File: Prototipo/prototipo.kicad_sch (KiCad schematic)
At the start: 13 parts, among them J1 Conn_01x02_Socket, J4 Conn_01x12_Pin

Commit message: cambio el zener y subo la listita de compras
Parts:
- J1: footprint TerminalBlock:TerminalBlock_MaiXu_MX126-5.0-02P_1x02_P5.00mm -> Huellas:TerminalBlock_bornier-2_P5.08mm
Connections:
- net GND is gone; now on net 0: A1.7 (GND), J4.1 (Pin_1), J4.12 (Pin_12)
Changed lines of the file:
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@@
+	(wire
+		(pts
+			(xy 147.32 175.26) (xy 146.05 175.26)
+		)
+		(stroke
+			(width 0)
+			(type default)
+		)
+	)
 	(wire
 		(pts
@@
 	(wire
 		(pts
-			(xy 146.05 175.26) (xy 148.59 175.26)
-		)
-		(stroke
-			(width 0)
-			(type default)
-		)
-	)
-	(wire
-		(pts
 			(xy 242.57 60.96) (xy 247.65 60.96)
 		)
@@
 		(pts
 			(xy 87.63 60.96) (xy 163.83 60.96)
+		)
+		(stroke
+			(width 0)
+			(type default)
+		)
+	)
+	(wire
+		(pts
+			(xy 147.32 180.34) (xy 147.32 175.26)
 		)
 		(stroke
@@
 				(path "/c9225433-a7fd-41e8-8162-e91e829dcb79"
 					(reference "#GND017")
-					(unit 1)
-				)
-			)
-		)
-	)
-	(symbol
-		(lib_id "power:GND")
-		(at 148.59 175.26 0)
-		(unit 1)
-		(exclude_from_sim no)
-		(in_bom yes)
-		(on_board yes)
-		(dnp no)
-		(fields_autoplaced yes)
-		(property "Reference" "#PWR01"
-			(at 148.59 181.61 0)
-			(effects
-				(font
-					(size 1.27 1.27)
-				)
-				(hide yes)
-			)
-		)
-		(property "Value" "GND"
-			(at 148.59 180.34 0)
-			(effects
-				(font
-					(size 1.27 1.27)
-				)
-			)
-		)
-		(property "Footprint" ""
-			(at 148.59 175.26 0)
-			(effects
-				(font
-					(size 1.27 1.27)
-				)
-				(hide yes)
-			)
-		)
-		(property "Datasheet" ""
-			(at 148.59 175.26 0)
-			(effects
-				(font
-					(size 1.27 1.27)
-				)
-				(hide yes)
-			)
-		)
-		(property "Description" "Power symbol creates a global label with name \"GND\" , ground"
-			(at 148.59 175.26 0)
-			(effects
-				(font
-					(size 1.27 1.27)
-				)
-				(hide yes)
-			)
-		)
-		(pin "1"
-		)
-		(instances
-			(project ""
-				(path "/c9225433-a7fd-41e8-8162-e91e829dcb79"
-					(reference "#PWR01")
 					(unit 1)
 				)
@@
 	)
 	(symbol
-		(lib_id "power:GND")
-		(at 88.9 182.88 0)
-		(unit 1)
-		(exclude_from_sim no)
-		(in_bom yes)
-		(on_board yes)
-		(dnp no)
-		(fields_autoplaced yes)
-		(property "Reference" "#PWR02"
-			(at 88.9 189.23 0)
-			(effects
-				(font
-					(size 1.27 1.27)
-				)
-				(hide yes)
-			)
-		)
-		(property "Value" "GND"
-			(at 88.9 187.96 0)
-			(effects
-				(font
-					(size 1.27 1.27)
-				)
-			)
-		)
-		(property "Footprint" ""
-			(at 88.9 182.88 0)
-			(effects
-				(font
-					(size 1.27 1.27)
-				)
-				(hide yes)
-			)
-		)
-		(property "Datasheet" ""
-			(at 88.9 182.88 0)
-			(effects
-				(font
-					(size 1.27 1.27)
-				)
-				(hide yes)
-			)
-		)
-		(property "Description" "Power symbol creates a global label with name \"GND\" , ground"
-			(at 88.9 182.88 0)
-			(effects
-				(font
-					(size 1.27 1.27)
-				)
-				(hide yes)
-			)
-		)
-		(pin "1"
-		)
-		(instances
-			(project "prototipo"
-				(path "/c9225433-a7fd-41e8-8162-e91e829dcb79"
-					(reference "#PWR02")
-					(unit 1)
-				)
-			)
-		)
-	)
-	(symbol
 		(lib_id "Connector:Conn_01x02_Socket")
 		(at 252.73 80.01 0)
@@
 			)
 		)
-		(property "Footprint" "TerminalBlock:TerminalBlock_MaiXu_MX126-5.0-02P_1x02_P5.00mm"
+		(property "Footprint" "Huellas:TerminalBlock_bornier-2_P5.08mm"
 			(at 252.73 80.01 0)
 			(effects
@@
 	)
 	(symbol
-		(lib_id "power:GND")
-		(at 81.28 156.21 0)
-		(unit 1)
-		(exclude_from_sim no)
-		(in_bom yes)
-		(on_board yes)
-		(dnp no)
-		(fields_autoplaced yes)
-		(property "Reference" "#PWR03"
-			(at 81.28 162.56 0)
-			(effects
-				(font
-					(size 1.27 1.27)
-				)
-				(hide yes)
-			)
-		)
-		(property "Value" "GND"
-			(at 81.28 161.29 0)
-			(effects
-				(font
-					(size 1.27 1.27)
-				)
-			)
-		)
-		(property "Footprint" ""
-			(at 81.28 156.21 0)
-			(effects
-				(font
-					(size 1.27 1.27)
-				)
-				(hide yes)
-			)
-		)
-		(property "Datasheet" ""
-			(at 81.28 156.21 0)
-			(effects
-				(font
-					(size 1.27 1.27)
-				)
-				(hide yes)
-			)
-		)
-		(property "Description" "Power symbol creates a global label with name \"GND\" , ground"
-			(at 81.28 156.21 0)
-			(effects
-				(font
-					(size 1.27 1.27)
-				)
-				(hide yes)
-			)
-		)
-		(pin "1"
-		)
-		(instances
-			(project "prototipo"
-				(path "/c9225433-a7fd-41e8-8162-e91e829dcb79"
-					(reference "#PWR03")
-					(unit 1)
-				)
-			)
-		)
-	)
-	(symbol
 		(lib_id "modificados:nmos")
 		(at 161.29 139.7 90)
@@
 	)
 	(symbol
+		(lib_id "ltspice:GND")
+		(at 81.28 156.21 0)
+		(unit 1)
+		(exclude_from_sim no)
+		(in_bom yes)
+		(on_board yes)
+		(dnp no)
+		(property "Reference" "#GND023"
+			(at 81.28 156.21 0)
+			(effects
+				(font
+					(size 1.27 1.27)
+				)
+				(hide yes)
+			)
+		)
+		(property "Value" "0"
+			(at 81.28 156.21 0)
+			(effects
+				(font
+					(size 1.0668 1.0668)
+				)
+				(hide yes)
+			)
+		)
+		(property "Footprint" ""
+			(at 81.28 156.21 0)
+			(effects
+				(font
+					(size 1.27 1.27)
+				)
+				(hide yes)
+			)
+		)
+		(property "Datasheet" ""
+			(at 81.28 156.21 0)
+			(effects
+				(font
+					(size 1.27 1.27)
+				)
+				(hide yes)
+			)
+		)
+		(property "Description" ""
+			(at 81.28 156.21 0)
+			(effects
+				(font
+					(size 1.27 1.27)
+				)
+				(hide yes)
+			)
+		)
+		(pin ""
+		)
+		(instances
+			(project "prototipo"
+				(path "/c9225433-a7fd-41e8-8162-e91e829dcb79"
+					(reference "#GND023")
+					(unit 1)
+				)
+			)
+		)
+	)
+	(symbol
 		(lib_id "Connector:Conn_01x12_Pin")
 		(at 95.25 168.91 180)
@@
 				)
 			)
+		)
+	)
+	(symbol
+		(lib_id "ltspice:GND")
+		(at 88.9 182.88 0)
+		(unit 1)
+		(exclude_from_sim no)
+		(in_bom yes)
+		(on_board yes)
+		(dnp no)
+		(property "Reference" "#GND022"
+			(at 88.9 182.88 0)
+			(effects
+				(font
+					(size 1.27 1.27)
+				)
+				(hide yes)
+			)
+		)
+		(property "Value" "0"
+			(at 88.9 182.88 0)
+			(effects
+				(font
+					(size 1.0668 1.0668)
+				)
+				(hide yes)
+			)
+		)
+		(property "Footprint" ""
+			(at 88.9 182.88 0)
+			(effects
+				(font
+					(size 1.27 1.27)
+				)
+				(hide yes)
+			)
+		)
+		(property "Datasheet" ""
+			(at 88.9 182.88 0)
+			(effects
+				(font
+					(size 1.27 1.27)
+				)
+				(hide yes)
+			)
+		)
+		(property "Description" ""
+			(at 88.9 182.88 0)
+			(effects
+				(font
+					(size 1.27 1.27)
+				)
+				(hide yes)
+			)
+		)
+		(pin ""
+		)
+		(instances
+			(project "prototipo"
+				(path "/c9225433-a7fd-41e8-8162-e91e829dcb79"
+					(reference "#GND022")
+					(unit 1)
+				)
+			)
+		)
+	)
+	(symbol
+		(lib_id "ltspice:GND")
+		(at 147.32 180.34 0)
+		(unit 1)
+		(exclude_from_sim no)
+		(in_bom yes)
+		(on_board yes)
+		(dnp no)
+		(property "Reference" "#GND024"
+			(at 147.32 180.34 0)
+			(effects
+				(font
+					(size 1.27 1.27)
+				)
+				(hide yes)
+			)
+		)
+		(property "Value" "0"
+			(at 147.32 180.34 0)
+			(effects
+				(font
+					(size 1.0668 1.0668)
+				)
+				(hide yes)
+			)
+		)
+		(property "Footprint" ""
+			(at 147.32 180.34 0)
+			(effects
+				(font
+					(size 1.27 1.27)
+				)
+				(hide yes)
+			)
+		)
+		(property "Datasheet" ""
+			(at 147.32 180.34 0)
+			(effects
+				(font
+					(size 1.27 1.27)
+				)
+				(hide yes)
+			)
+		)
+		(property "Description" ""
+			(at 147.32 180.34 0)
+			(effects
+				(font
+					(size 1.27 1.27)
+				)
+				(hide yes)
+			)
+		)
+		(pin ""
+		)
+		(instances
+			(project "prototipo"
+				(path "/c9225433-a7fd-41e8-8162-e91e829dcb79"
+					(reference "#GND024")
+					(unit 1)
+				)
+			)

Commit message: termino de reacomodar las celdas con la disposición nueva, faltan las conexiones de la entrada.
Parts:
- renumbered J4 to IN1, J1 to OUT1, SGND11 to Sgnd11, SGND1 to Sgnd21, TP1 to TPbanco1, TP2 to TPbanco2
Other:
- sheet celda_1 renamed celda_11
- sheet celda_2 renamed celda_12
- sheet celda_3 renamed celda_21
- sheet celda_4 renamed celda_22
- sheet celda_5 renamed celda_31
- sheet celda_6 renamed celda_32
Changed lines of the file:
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@@
 		(dnp no)
 		(fields_autoplaced yes)
-		(property "Reference" "J1"
+		(property "Reference" "OUT1"
 			(at 254 80.0099 0)
 			(effects
@@
 			(project "prototipo"
 				(path "/c9225433-a7fd-41e8-8162-e91e829dcb79"
-					(reference "J1")
+					(reference "OUT1")
 					(unit 1)
 				)
@@
 		(dnp no)
 		(fields_autoplaced yes)
-		(property "Reference" "TP2"
-			(at 231.287 56.3879 0)
+		(property "Reference" "TPbanco2"
+			(at 231.14 56.3879 0)
 			(effects
 				(font
@@
 		)
 		(property "Value" "TestPoint"
-			(at 231.287 58.9279 0)
+			(at 231.14 58.9279 0)
 			(effects
 				(font
@@
 			(project "prototipo"
 				(path "/c9225433-a7fd-41e8-8162-e91e829dcb79"
-					(reference "TP2")
+					(reference "TPbanco2")
 					(unit 1)
 				)
@@
 		(on_board yes)
 		(dnp no)
-		(property "Reference" "SGND11"
+		(property "Reference" "Sgnd11"
 			(at 86.36 135.255 0)
 			(effects
@@
 			(project "prototipo"
 				(path "/c9225433-a7fd-41e8-8162-e91e829dcb79"
-					(reference "SGND11")
+					(reference "Sgnd11")
 					(unit 1)
 				)
@@
 		(on_board yes)
 		(dnp no)
-		(property "Reference" "SGND1"
+		(property "Reference" "Sgnd21"
 			(at 163.83 135.255 0)
 			(effects
@@
 			(project "prototipo"
 				(path "/c9225433-a7fd-41e8-8162-e91e829dcb79"
-					(reference "SGND1")
+					(reference "Sgnd21")
 					(unit 1)
 				)
@@
 		(dnp no)
 		(fields_autoplaced yes)
-		(property "Reference" "J4"
+		(property "Reference" "IN1"
 			(at 96.52 166.3699 0)
 			(effects
@@
 			(project ""
 				(path "/c9225433-a7fd-41e8-8162-e91e829dcb79"
-					(reference "J4")
+					(reference "IN1")
 					(unit 1)
 				)
@@
 		(dnp no)
 		(fields_autoplaced yes)
-		(property "Reference" "TP1"
+		(property "Reference" "TPbanco1"
 			(at 224.79 91.9479 0)
 			(effects
@@
 			(project "prototipo"
 				(path "/c9225433-a7fd-41e8-8162-e91e829dcb79"
-					(reference "TP1")
+					(reference "TPbanco1")
 					(unit 1)
 				)
@@
 			(color 0 0 0 0.0000)
 		)
-		(property "Sheetname" "celda_6"
+		(property "Sheetname" "celda_32"
 			(at 135.89 33.5784 0)
 			(show_name yes)
@@
 			(color 0 0 0 0.0000)
 		)
-		(property "Sheetname" "celda_2"
+		(property "Sheetname" "celda_12"
 			(at 135.89 99.6184 0)
 			(show_name yes)
@@
 			(color 0 0 0 0.0000)
 		)
-		(property "Sheetname" "celda_3"
+		(property "Sheetname" "celda_21"
 			(at 59.69 64.0584 0)
 			(show_name yes)
@@
 			(color 0 0 0 0.0000)
 		)
-		(property "Sheetname" "celda_4"
+		(property "Sheetname" "celda_22"
 			(at 135.89 64.0584 0)
 			(show_name yes)
@@
 			(color 0 0 0 0.0000)
 		)
-		(property "Sheetname" "celda_1"
+		(property "Sheetname" "celda_11"
 			(at 59.69 99.6184 0)
 			(show_name yes)
@@
 			(color 0 0 0 0.0000)
 		)
-		(property "Sheetname" "celda_5"
+		(property "Sheetname" "celda_31"
 			(at 59.69 33.5784 0)
 			(show_name yes)

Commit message: Propuesta de conexión de las entradas
no me gusta la opción, pero esta conectado
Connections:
- net Vc_12: now also IN1.8 (Pin_8); no longer IN1.6 (Pin_6)
- net Vc_32: now also IN1.6 (Pin_6); no longer IN1.8 (Pin_8)
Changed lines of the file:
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@@
+		)
+	)
+	(global_label "Vc_22"
+		(shape bidirectional)
+		(at 90.17 166.37 180)
+		(effects
+			(font
+				(size 1.0668 1.0668)
+			)
+			(justify right)
+		)
+		(property "Intersheetrefs" "${INTERSHEET_REFS}"
+			(at 90.17 166.37 0)
+			(effects
+				(font
+					(size 1.27 1.27)
+				)
+				(hide yes)
+			)
 		)
 	)
@@
 		)
 	)
+	(global_label "Vc_32"
+		(shape bidirectional)
+		(at 90.17 168.91 180)
+		(effects
+			(font
+				(size 1.0668 1.0668)
+			)
+			(justify right)
+		)
+		(property "Intersheetrefs" "${INTERSHEET_REFS}"
+			(at 90.17 168.91 0)
+			(effects
+				(font
+					(size 1.27 1.27)
+				)
+				(hide yes)
+			)
+		)
+	)
 	(global_label "Vc2"
 		(shape bidirectional)
@@
 		)
 	)
-	(global_label "Vc_22"
+	(global_label "Vc_12"
 		(shape bidirectional)
-		(at 90.17 166.37 180)
+		(at 90.17 163.83 180)
 		(effects
 			(font
@@
 		)
 		(property "Intersheetrefs" "${INTERSHEET_REFS}"
-			(at 90.17 166.37 0)
+			(at 90.17 163.83 0)
 			(effects
 				(font
@@
 		)
 	)
-	(global_label "Vc_12"
-		(shape bidirectional)
-		(at 90.17 168.91 180)
-		(effects
-			(font
-				(size 1.0668 1.0668)
-			)
-			(justify right)
-		)
-		(property "Intersheetrefs" "${INTERSHEET_REFS}"
-			(at 90.17 168.91 0)
-			(effects
-				(font
-					(size 1.27 1.27)
-				)
-				(hide yes)
-			)
-		)
-	)
 	(global_label "Vc_11"
 		(shape bidirectional)
@@
 		)
 	)
-	(global_label "Vc_32"
-		(shape bidirectional)
-		(at 90.17 163.83 180)
-		(effects
-			(font
-				(size 1.0668 1.0668)
-			)
-			(justify right)
-		)
-		(property "Intersheetrefs" "${INTERSHEET_REFS}"
-			(at 90.17 163.83 0)
-			(effects
-				(font
-					(size 1.27 1.27)
-				)
-				(hide yes)
-			)
-		)
-	)
-	(symbol
-		(lib_id "ltspice:GND")
+	(symbol
+		(lib_id "power:GND")
 		(at 62.23 163.83 0)
 		(unit 1)
@@
 			)
 		)
-		(property "Description" ""
+		(property "Description" "Power symbol creates a global label with name \"GND\" , ground"
 			(at 62.23 163.83 0)
 			(effects
@@
 			)
 		)
-		(pin ""
+		(pin "1"
 		)
 		(instances
@@
 	)
 	(symbol
-		(lib_id "ltspice:GND")
+		(lib_id "power:GND")
 		(at 171.45 140.97 0)
 		(unit 1)
@@
 			)
 		)
-		(property "Description" ""
+		(property "Description" "Power symbol creates a global label with name \"GND\" , ground"
 			(at 171.45 140.97 0)
 			(effects
@@
 			)
 		)
-		(pin ""
+		(pin "1"
 		)
 		(instances
@@
 	)
 	(symbol
-		(lib_id "ltspice:GND")
+		(lib_id "power:GND")
 		(at 48.26 163.83 0)
 		(unit 1)
@@
 			)
 		)
-		(property "Description" ""
+		(property "Description" "Power symbol creates a global label with name \"GND\" , ground"
 			(at 48.26 163.83 0)
 			(effects
@@
 			)
 		)
-		(pin ""
+		(pin "1"
 		)
 		(instances
@@
 	)
 	(symbol
-		(lib_id "ltspice:GND")
+		(lib_id "power:GND")
 		(at 81.28 156.21 0)
 		(unit 1)
@@
 			)
 		)
-		(property "Description" ""
+		(property "Description" "Power symbol creates a global label with name \"GND\" , ground"
 			(at 81.28 156.21 0)
 			(effects
@@
 			)
 		)
-		(pin ""
+		(pin "1"
 		)
 		(instances
@@
 	)
 	(symbol
-		(lib_id "ltspice:GND")
+		(lib_id "power:GND")
 		(at 19.05 163.83 0)
 		(unit 1)
@@
 			)
 		)
-		(property "Description" ""
+		(property "Description" "Power symbol creates a global label with name \"GND\" , ground"
 			(at 19.05 163.83 0)
 			(effects
@@
 			)
 		)
-		(pin ""
+		(pin "1"
 		)
 		(instances
@@
 	)
 	(symbol
-		(lib_id "ltspice:GND")
+		(lib_id "power:GND")
 		(at 95.25 139.7 0)
 		(unit 1)
@@
 			)
 		)
-		(property "Description" ""
+		(property "Description" "Power symbol creates a global label with name \"GND\" , ground"
 			(at 95.25 139.7 0)
 			(effects
@@
 			)
 		)
-		(pin ""
+		(pin "1"
 		)
 		(instances
@@
 	)
 	(symbol
-		(lib_id "ltspice:GND")
+		(lib_id "power:GND")
 		(at 88.9 182.88 0)
 		(unit 1)
@@
 			)
 		)
-		(property "Description" ""
+		(property "Description" "Power symbol creates a global label with name \"GND\" , ground"
 			(at 88.9 182.88 0)
 			(effects
@@
 			)
 		)
-		(pin ""
+		(pin "1"
 		)
 		(instances
@@
 	)
 	(symbol
-		(lib_id "ltspice:GND")
+		(lib_id "power:GND")
 		(at 147.32 180.34 0)
 		(unit 1)
@@
 			)
 		)
-		(property "Description" ""
+		(property "Description" "Power symbol creates a global label with name \"GND\" , ground"
 			(at 147.32 180.34 0)
 			(effects
@@
 			)
 		)
-		(pin ""
+		(pin "1"
 		)
 		(instances
@@
 	)
 	(symbol
-		(lib_id "ltspice:GND")
+		(lib_id "power:GND")
 		(at 34.29 163.83 0)
 		(unit 1)
@@
 			)
 		)
-		(property "Description" ""
+		(property "Description" "Power symbol creates a global label with name \"GND\" , ground"
 			(at 34.29 163.83 0)
 			(effects
@@
 			)
 		)
-		(pin ""
-		)
-		(instances
+		(pin "1"
+		)
+		(instances

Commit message: primer propuesta de conexion de entradas
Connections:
- net 0: no longer IN1.12 (Pin_12)
- net VCC: now also IN1.12 (Pin_12); no longer IN1.2 (Pin_2)
- net Vc1: now also IN1.11 (Pin_11); no longer IN1.9 (Pin_9)
- net Vc3: now also IN1.9 (Pin_9); no longer IN1.11 (Pin_11)
- net Vc_11: now also IN1.4 (Pin_4); no longer IN1.3 (Pin_3)
- net Vc_21: now also IN1.3 (Pin_3); no longer IN1.4 (Pin_4)

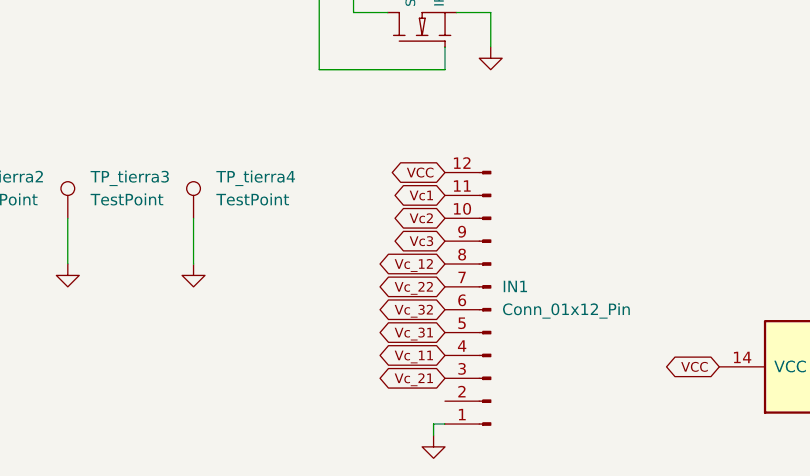
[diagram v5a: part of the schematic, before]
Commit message: acomodo la bornera
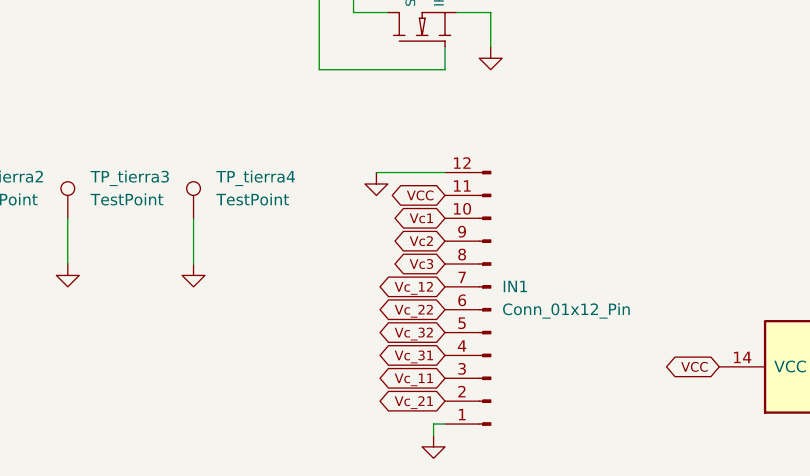
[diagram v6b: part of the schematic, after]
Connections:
- net 0: now also IN1.12 (Pin_12)
- net VCC: now also IN1.11 (Pin_11); no longer IN1.12 (Pin_12)
- net Vc1: now also IN1.10 (Pin_10); no longer IN1.11 (Pin_11)
- net Vc2: now also IN1.9 (Pin_9); no longer IN1.10 (Pin_10)
- net Vc3: now also IN1.8 (Pin_8); no longer IN1.9 (Pin_9)
- net Vc_11: now also IN1.3 (Pin_3); no longer IN1.4 (Pin_4)
- net Vc_12: now also IN1.7 (Pin_7); no longer IN1.8 (Pin_8)
- net Vc_21: now also IN1.2 (Pin_2); no longer IN1.3 (Pin_3)
- net Vc_22: now also IN1.6 (Pin_6); no longer IN1.7 (Pin_7)
- net Vc_31: now also IN1.4 (Pin_4); no longer IN1.5 (Pin_5)
- net Vc_32: now also IN1.5 (Pin_5); no longer IN1.6 (Pin_6)
